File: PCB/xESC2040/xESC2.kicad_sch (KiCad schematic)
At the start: 31 parts, among them J1 Conn_01x06_Male, J2 U254-051T-4BH83-F1S, J3 Conn_01x05_Male, J4 Conn_01x05_Male

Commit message: Change part for J5 to be a 9 pin header so can be soldered along with J1 to ease assembly - J1 marked as DNP
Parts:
- J1: Config (none) -> do not place
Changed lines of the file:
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@@
+      (effects (font (size 1.27 1.27)) hide)
+    )
+    (property "Config" "do not place" (id 7) (at 21.59 115.57 0)
       (effects (font (size 1.27 1.27)) hide)
     )

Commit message: Fixed #5
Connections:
- net +3V3: now also R12.1, R8.1, R9.1
- net +5V: no longer R12.1, R8.1, R9.1
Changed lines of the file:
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@@
   (junction (at 48.26 53.34) (diameter 0) (color 0 0 0 0)
   )
+  (junction (at 36.83 95.25) (diameter 0) (color 0 0 0 0)
+  )
   (junction (at 129.54 168.91) (diameter 0) (color 0 0 0 0)
   )
@@
   )
   (junction (at 52.07 120.65) (diameter 0) (color 0 0 0 0)
-  )
-  (junction (at 31.75 95.25) (diameter 0) (color 0 0 0 0)
   )
   (junction (at 46.99 95.25) (diameter 0) (color 0 0 0 0)
@@
     (stroke (width 0) (type default) (color 0 0 0 0))
   )
-  (wire (pts (xy 31.75 95.25) (xy 31.75 90.17))
-    (stroke (width 0) (type default) (color 0 0 0 0))
-  )
   (wire (pts (xy 90.805 93.345) (xy 115.57 93.345))
     (stroke (width 0) (type default) (color 0 0 0 0))
@@
     (stroke (width 0) (type default) (color 0 0 0 0))
   )
-  (wire (pts (xy 31.75 95.25) (xy 41.91 95.25))
-    (stroke (width 0) (type default) (color 0 0 0 0))
-  )
   (wire (pts (xy 217.17 39.37) (xy 223.52 39.37))
     (stroke (width 0) (type default) (color 0 0 0 0))
@@
     (stroke (width 0) (type default) (color 0 0 0 0))
   )
+  (wire (pts (xy 36.83 95.25) (xy 41.91 95.25))
+    (stroke (width 0) (type default) (color 0 0 0 0))
+  )
   (wire (pts (xy 129.54 158.75) (xy 129.54 154.94))
     (stroke (width 0) (type default) (color 0 0 0 0))
@@
     (stroke (width 0) (type default) (color 0 0 0 0))
   )
+  (wire (pts (xy 36.83 95.25) (xy 36.83 90.17))
+    (stroke (width 0) (type default) (color 0 0 0 0))
+  )
   (wire (pts (xy 48.26 53.34) (xy 48.26 59.69))
     (stroke (width 0) (type default) (color 0 0 0 0))
@@
     (stroke (width 0) (type default) (color 0 0 0 0))
   )
-  (wire (pts (xy 36.83 104.14) (xy 36.83 90.17))
+  (wire (pts (xy 36.83 104.14) (xy 36.83 95.25))
     (stroke (width 0) (type default) (color 0 0 0 0))
   )
@@
     (stroke (width 0) (type default) (color 0 0 0 0))
   )
-  (wire (pts (xy 31.75 110.49) (xy 31.75 95.25))
-    (stroke (width 0) (type default) (color 0 0 0 0))
-  )
+  (wire (pts (xy 31.75 90.17) (xy 31.75 110.49))
+    (stroke (width 0) (type default) (color 0 0 0 0))
+  )

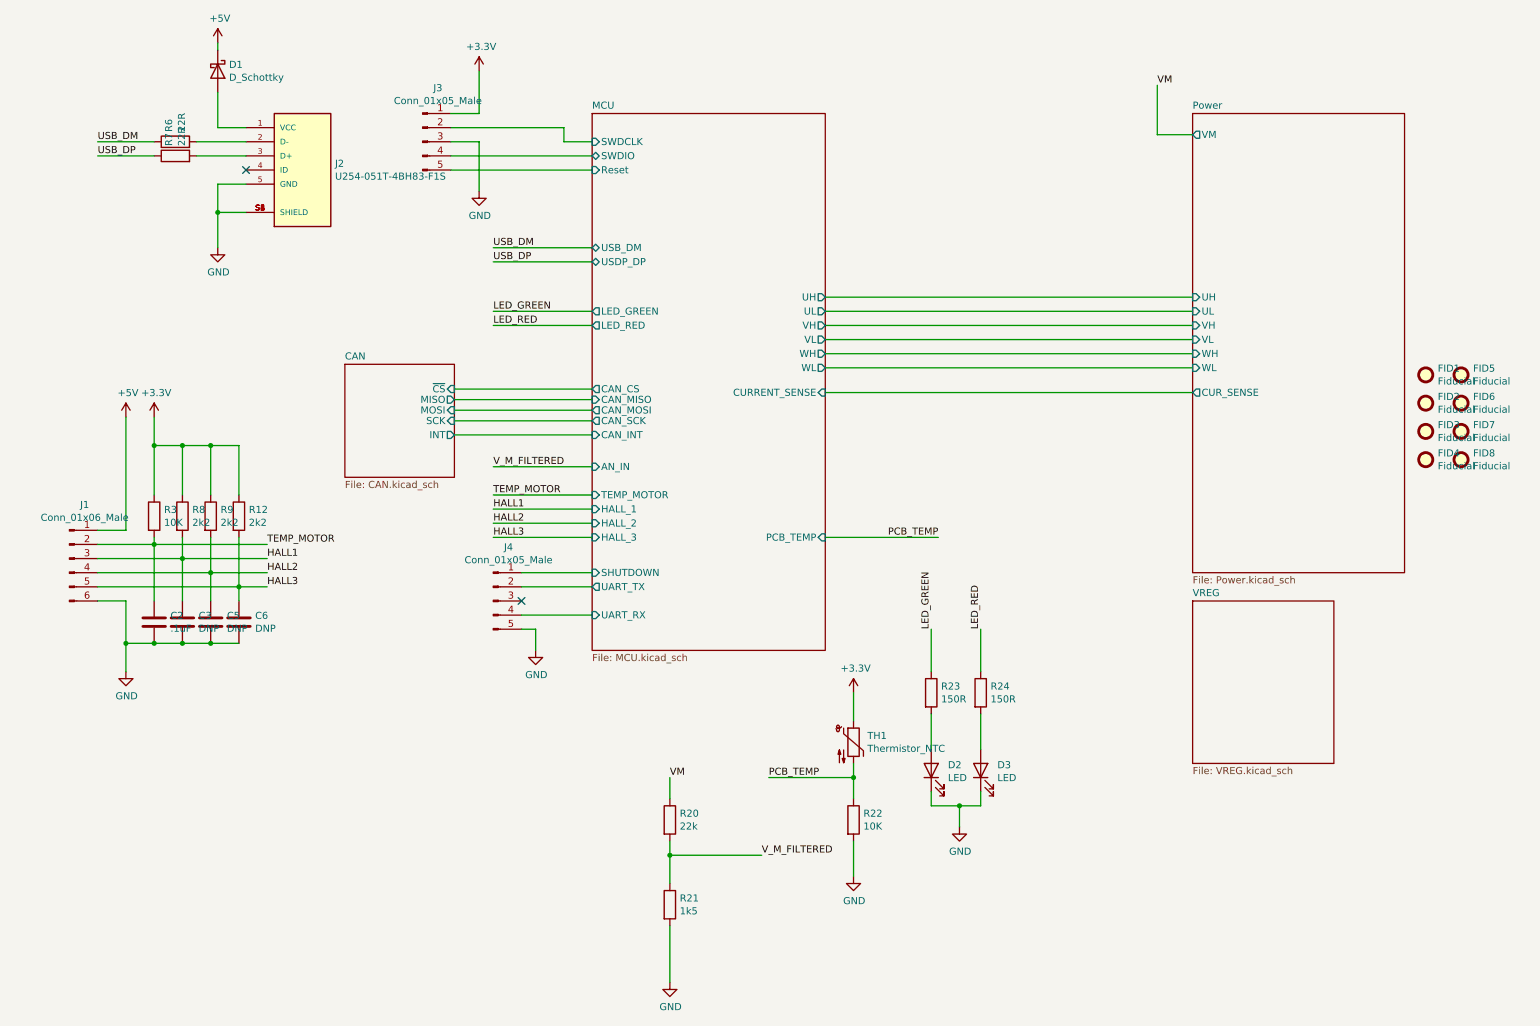
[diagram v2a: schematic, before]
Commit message: Merge J5 and J1 into one connector - no pinout changes or connector move
With J5 gone had kicad redo  reference designators - hope that's ok
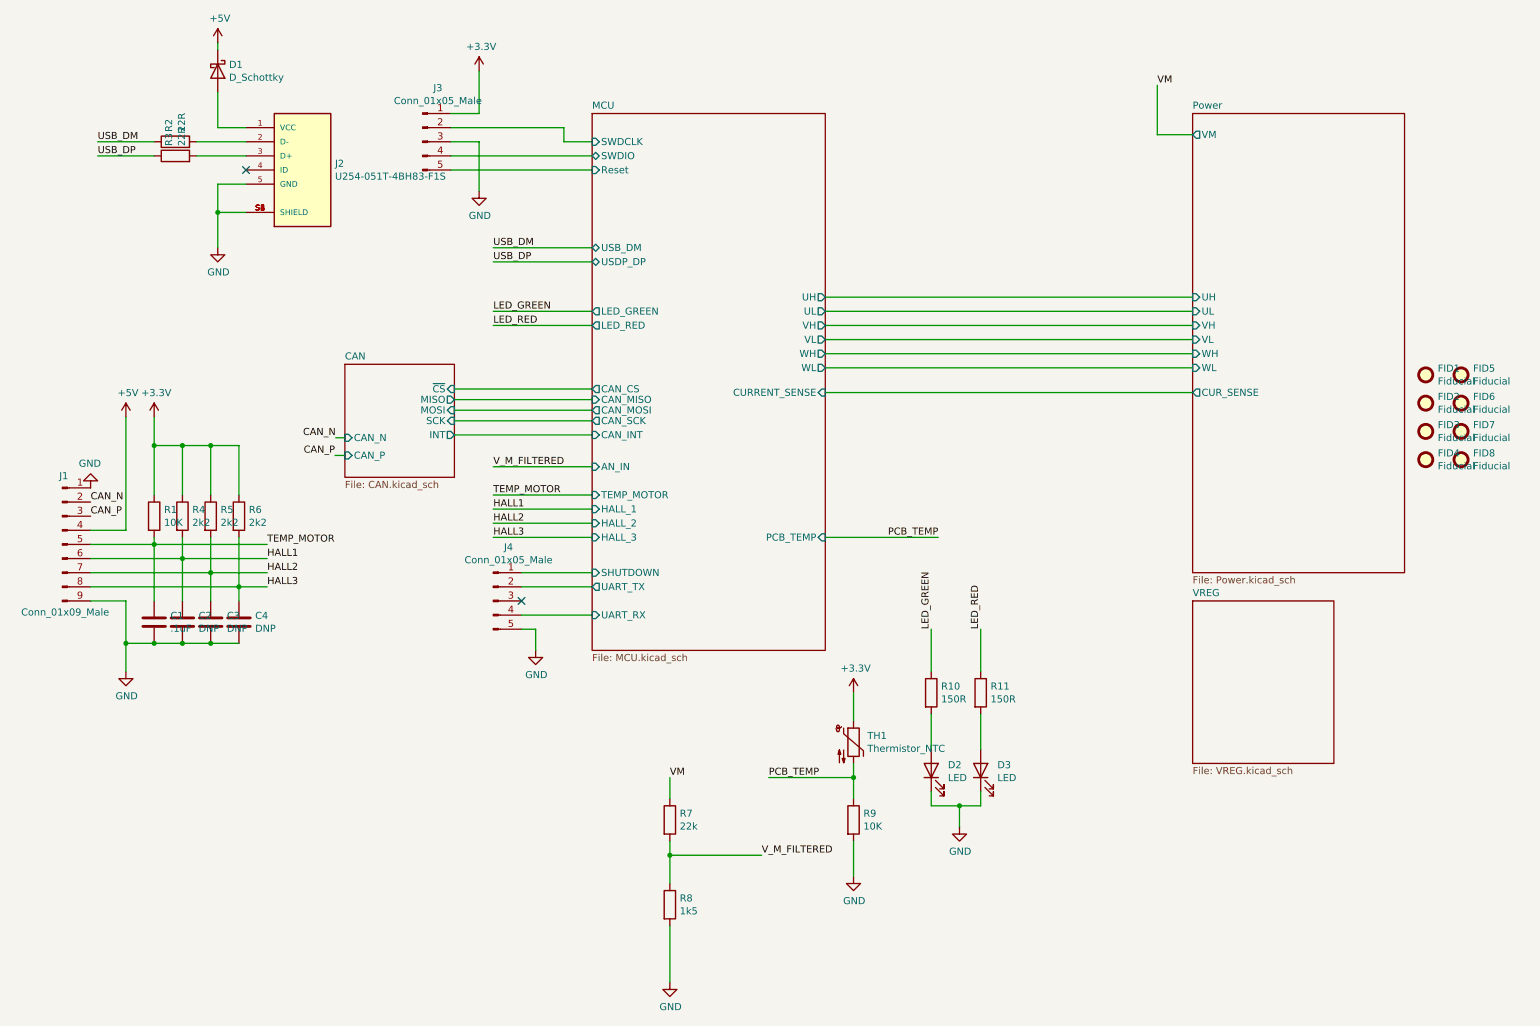
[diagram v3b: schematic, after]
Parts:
- removed J1: Conn_01x06_Male, Connector_PinHeader_2.54mm:PinHeader_1x06_P2.54mm_Vertical, symbol Connector:Conn_01x06_Male
- added J1: Conn_01x09_Male, Connector_PinHeader_2.54mm:PinHeader_1x09_P2.54mm_Vertical, symbol Connector:Conn_01x09_Male
- renumbered C2 to C1, C3 to C2, C5 to C3, C6 to C4, R3 to R1, R23 to R10, R24 to R11, R6 to R2, R7 to R3, R8 to R4, R9 to R5, R12 to R6, R20 to R7, R21 to R8, R22 to R9
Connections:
- net +5V: now also J1.4 (Pin_4)
- net GND: now also J1.1 (Pin_1), J1.9 (Pin_9)
- net HALL1: now also J1.6 (Pin_6)
- net HALL2: now also J1.7 (Pin_7)
- net HALL3: now also J1.8 (Pin_8)
- net TEMP_MOTOR: now also J1.5 (Pin_5)
- new net CAN_N: J1.2 (Pin_2)
- new net CAN_P: J1.3 (Pin_3)
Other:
- sheet CAN ports: added CAN_N, CAN_P; removed none

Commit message: BoM data updates
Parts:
- R1, R9: Digikey RC0603FR-0710KL -> 311-10.0KHRCT-ND; Part Number 311-10.0KHRCT-ND -> RC0603FR-0710KL
- R10, R11: Digikey RC0603FR-07150RL -> 311-150HRCT-ND; Part Number 311-150HRCT-ND -> RC0603FR-07150RL
- R2, R3: Digikey RMCF0603FT22R0 -> RMCF0603FT22R0CT-ND; Part Number RMCF0603FT22R0CT-ND -> RMCF0603FT22R0
- R4, R5, R6: Digikey RC0603FR-072K2L -> 311-2.20KHRCT-ND; Part Number 311-2.20KHRCT-ND -> RC0603FR-072K2L
- R7: Digikey RMCF0603FT22K0 -> RMCF0603FT22K0CT-ND; Part Number RMCF0603FT22K0CT-ND -> RMCF0603FT22K0
- R8: Digikey RC0603FR-071K5L -> 311-1.50KHRCT-ND; Part Number 311-1.50KHRCT-ND -> RC0603FR-071K5L
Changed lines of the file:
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@@
       (effects (font (size 1.27 1.27)) hide)
     )
-    (property "Digikey" "RC0603FR-0710KL" (id 4) (at 36.83 107.95 0)
-      (effects (font (size 1.27 1.27)) hide)
-    )
-    (property "Part Number" "311-10.0KHRCT-ND" (id 5) (at 36.83 107.95 0)
+    (property "Digikey" "311-10.0KHRCT-ND" (id 4) (at 36.83 107.95 0)
+      (effects (font (size 1.27 1.27)) hide)
+    )
+    (property "Part Number" "RC0603FR-0710KL" (id 5) (at 36.83 107.95 0)
       (effects (font (size 1.27 1.27)) hide)
     )
@@
       (effects (font (size 1.27 1.27)) hide)
     )
-    (property "Digikey" "RC0603FR-072K2L" (id 4) (at 41.91 107.95 0)
-      (effects (font (size 1.27 1.27)) hide)
-    )
-    (property "Part Number" "311-2.20KHRCT-ND" (id 5) (at 41.91 107.95 0)
+    (property "Digikey" "311-2.20KHRCT-ND" (id 4) (at 41.91 107.95 0)
+      (effects (font (size 1.27 1.27)) hide)
+    )
+    (property "Part Number" "RC0603FR-072K2L" (id 5) (at 41.91 107.95 0)
       (effects (font (size 1.27 1.27)) hide)
     )
@@
       (effects (font (size 1.27 1.27)) hide)
     )
-    (property "Digikey" "RC0603FR-072K2L" (id 4) (at 46.99 107.95 0)
-      (effects (font (size 1.27 1.27)) hide)
-    )
-    (property "Part Number" "311-2.20KHRCT-ND" (id 5) (at 46.99 107.95 0)
+    (property "Digikey" "311-2.20KHRCT-ND" (id 4) (at 46.99 107.95 0)
+      (effects (font (size 1.27 1.27)) hide)
+    )
+    (property "Part Number" "RC0603FR-072K2L" (id 5) (at 46.99 107.95 0)
       (effects (font (size 1.27 1.27)) hide)
     )
@@
       (effects (font (size 1.27 1.27)) hide)
     )
-    (property "Digikey" "RC0603FR-072K2L" (id 4) (at 52.07 107.95 0)
-      (effects (font (size 1.27 1.27)) hide)
-    )
-    (property "Part Number" "311-2.20KHRCT-ND" (id 5) (at 52.07 107.95 0)
+    (property "Digikey" "311-2.20KHRCT-ND" (id 4) (at 52.07 107.95 0)
+      (effects (font (size 1.27 1.27)) hide)
+    )
+    (property "Part Number" "RC0603FR-072K2L" (id 5) (at 52.07 107.95 0)
       (effects (font (size 1.27 1.27)) hide)
     )
@@
       (effects (font (size 1.27 1.27)) hide)
     )
-    (property "Digikey" "RMCF0603FT22K0" (id 4) (at 129.54 162.56 0)
-      (effects (font (size 1.27 1.27)) hide)
-    )
-    (property "Part Number" "RMCF0603FT22K0CT-ND" (id 5) (at 129.54 162.56 0)
+    (property "Digikey" "RMCF0603FT22K0CT-ND" (id 4) (at 129.54 162.56 0)
+      (effects (font (size 1.27 1.27)) hide)
+    )
+    (property "Part Number" "RMCF0603FT22K0" (id 5) (at 129.54 162.56 0)
       (effects (font (size 1.27 1.27)) hide)
     )
@@
       (effects (font (size 1.27 1.27)) hide)
     )
-    (property "Digikey" "RC0603FR-071K5L" (id 4) (at 129.54 177.8 0)
-      (effects (font (size 1.27 1.27)) hide)
-    )
-    (property "Part Number" "311-1.50KHRCT-ND" (id 5) (at 129.54 177.8 0)
+    (property "Digikey" "311-1.50KHRCT-ND" (id 4) (at 129.54 177.8 0)
+      (effects (font (size 1.27 1.27)) hide)
+    )
+    (property "Part Number" "RC0603FR-071K5L" (id 5) (at 129.54 177.8 0)
       (effects (font (size 1.27 1.27)) hide)
     )
@@
       (effects (font (size 1.27 1.27)) hide)
     )
-    (property "Digikey" "RMCF0603FT22R0" (id 4) (at 40.64 43.18 0)
-      (effects (font (size 1.27 1.27)) hide)
-    )
-    (property "Part Number" "RMCF0603FT22R0CT-ND" (id 5) (at 40.64 43.18 0)
+    (property "Digikey" "RMCF0603FT22R0CT-ND" (id 4) (at 40.64 43.18 0)
+      (effects (font (size 1.27 1.27)) hide)
+    )
+    (property "Part Number" "RMCF0603FT22R0" (id 5) (at 40.64 43.18 0)
       (effects (font (size 1.27 1.27)) hide)
     )
@@
       (effects (font (size 1.27 1.27)) hide)
     )
-    (property "Digikey" "RMCF0603FT22R0" (id 4) (at 40.64 40.64 0)
-      (effects (font (size 1.27 1.27)) hide)
-    )
-    (property "Part Number" "RMCF0603FT22R0CT-ND" (id 5) (at 40.64 40.64 0)
+    (property "Digikey" "RMCF0603FT22R0CT-ND" (id 4) (at 40.64 40.64 0)
+      (effects (font (size 1.27 1.27)) hide)
+    )
+    (property "Part Number" "RMCF0603FT22R0" (id 5) (at 40.64 40.64 0)
       (effects (font (size 1.27 1.27)) hide)
     )
@@
       (effects (font (size 1.27 1.27)) hide)
     )
-    (property "Digikey" "RC0603FR-07150RL" (id 4) (at 176.53 139.7 0)
-      (effects (font (size 1.27 1.27)) hide)
-    )
-    (property "Part Number" "311-150HRCT-ND" (id 5) (at 176.53 139.7 0)
+    (property "Digikey" "311-150HRCT-ND" (id 4) (at 176.53 139.7 0)
+      (effects (font (size 1.27 1.27)) hide)
+    )
+    (property "Part Number" "RC0603FR-07150RL" (id 5) (at 176.53 139.7 0)
       (effects (font (size 1.27 1.27)) hide)
     )
@@
       (effects (font (size 1.27 1.27)) hide)
     )
-    (property "Digikey" "RC0603FR-0710KL" (id 4) (at 162.56 162.56 0)
-      (effects (font (size 1.27 1.27)) hide)
-    )
-    (property "Part Number" "311-10.0KHRCT-ND" (id 5) (at 162.56 162.56 0)
+    (property "Digikey" "311-10.0KHRCT-ND" (id 4) (at 162.56 162.56 0)
+      (effects (font (size 1.27 1.27)) hide)
+    )
+    (property "Part Number" "RC0603FR-0710KL" (id 5) (at 162.56 162.56 0)
       (effects (font (size 1.27 1.27)) hide)
     )
@@
       (effects (font (size 1.27 1.27)) hide)
     )
-    (property "Digikey" "RC0603FR-07150RL" (id 4) (at 185.42 139.7 0)
-      (effects (font (size 1.27 1.27)) hide)
-    )
-    (property "Part Number" "311-150HRCT-ND" (id 5) (at 185.42 139.7 0)
-      (effects (font (size 1.27 1.27)) hide)
-    )
+    (property "Digikey" "311-150HRCT-ND" (id 4) (at 185.42 139.7 0)
+      (effects (font (size 1.27 1.27)) hide)
+    )
+    (property "Part Number" "RC0603FR-07150RL" (id 5) (at 185.42 139.7 0)
+      (effects (font (size 1.27 1.27)) hide)
+    )

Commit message: wip
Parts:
- C1: Digikey 490-1331-1-ND -> 1276-1935-1-ND
- D2: value LED -> LED GREEN
- D3: value LED -> LED RED
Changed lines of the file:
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@@
       (effects (font (size 1.27 1.27)) hide)
     )
-    (property "Digikey" "490-1331-1-ND" (id 4) (at 36.83 127 0)
+    (property "Digikey" "1276-1935-1-ND" (id 4) (at 36.83 127 0)
       (effects (font (size 1.27 1.27)) hide)
     )
@@
       (effects (font (size 1.27 1.27)) (justify right))
     )
-    (property "Value" "LED" (id 1) (at 179.5272 154.9908 90)
+    (property "Value" "LED GREEN" (id 1) (at 179.5272 154.9908 90)
       (effects (font (size 1.27 1.27)) (justify right))
     )
@@
       (effects (font (size 1.27 1.27)) (justify right))
     )
-    (property "Value" "LED" (id 1) (at 188.4172 154.9908 90)
+    (property "Value" "LED RED" (id 1) (at 188.4172 154.9908 90)
       (effects (font (size 1.27 1.27)) (justify right))
     )
@@
     )
     (path "/00000000-0000-0000-0000-000061a3f4e8/b5bb664c-0ca2-4020-8c91-65a02cddeb94"
-      (reference "C20") (unit 1) (value "TODO") (footprint "Capacitor_SMD:C_0603_1608Metric")
+      (reference "C20") (unit 1) (value ".1uF") (footprint "Capacitor_SMD:C_0603_1608Metric")
     )
     (path "/00000000-0000-0000-0000-000061a3f4e8/00000000-0000-0000-0000-000061a4478e"
-      (reference "C21") (unit 1) (value "TODO") (footprint "Capacitor_SMD:C_0603_1608Metric")
+      (reference "C21") (unit 1) (value "470nF{slash}16V") (footprint "Capacitor_SMD:C_0603_1608Metric")
     )
     (path "/00000000-0000-0000-0000-000061a3f4e8/00000000-0000-0000-0000-000061a4b0d8"
-      (reference "C22") (unit 1) (value "TODO") (footprint "Capacitor_SMD:C_0603_1608Metric")
+      (reference "C22") (unit 1) (value "470nF{slash}16V") (footprint "Capacitor_SMD:C_0603_1608Metric")
     )
     (path "/00000000-0000-0000-0000-000061a3f4e8/00000000-0000-0000-0000-000061a4bb26"
-      (reference "C23") (unit 1) (value "TODO") (footprint "Capacitor_SMD:C_0603_1608Metric")
+      (reference "C23") (unit 1) (value "470nF{slash}16V") (footprint "Capacitor_SMD:C_0603_1608Metric")
     )
     (path "/00000000-0000-0000-0000-000061e7227a/00000000-0000-0000-0000-000061e808d2"
-      (reference "C24") (unit 1) (value "10uF/16V") (footprint "Capacitor_SMD:C_0603_1608Metric")
+      (reference "C24") (unit 1) (value "4.7uF{slash}16V") (footprint "Capacitor_SMD:C_0603_1608Metric")
     )
     (path "/00000000-0000-0000-0000-000061e7227a/6c7a9801-3387-4fa6-ac74-fb6a0114bfa0"
-      (reference "C25") (unit 1) (value "10uF/16V") (footprint "Capacitor_SMD:C_0603_1608Metric")
+      (reference "C25") (unit 1) (value "4.7uF{slash}16V") (footprint "Capacitor_SMD:C_0603_1608Metric")
     )
     (path "/00000000-0000-0000-0000-000061a3f4e8/00000000-0000-0000-0000-000061a57dd0/00000000-0000-0000-0000-000061a5475a"
@@
     )
     (path "/00000000-0000-0000-0000-000061e2e723"
-      (reference "D2") (unit 1) (value "LED") (footprint "LED_SMD:LED_0603_1608Metric")
+      (reference "D2") (unit 1) (value "LED GREEN") (footprint "LED_SMD:LED_0603_1608Metric")
     )
     (path "/00000000-0000-0000-0000-000061e3947a"
-      (reference "D3") (unit 1) (value "LED") (footprint "LED_SMD:LED_0603_1608Metric")
+      (reference "D3") (unit 1) (value "LED RED") (footprint "LED_SMD:LED_0603_1608Metric")
     )
     (path "/00000000-0000-0000-0000-00006251351c"
@@
     )
     (path "/00000000-0000-0000-0000-000061a3f4e8/363f2f39-147c-4fe7-ae7c-93ceb80426de"
-      (reference "R17") (unit 1) (value "TODO") (footprint "Resistor_SMD:R_0603_1608Metric")
+      (reference "R17") (unit 1) (value "DNP") (footprint "Resistor_SMD:R_0603_1608Metric")
     )
     (path "/00000000-0000-0000-0000-000061a3f4e8/c6c90108-6f77-4a49-81b5-720115855806"
-      (reference "R18") (unit 1) (value "33mR") (footprint "Resistor_SMD:R_2512_6332Metric")
+      (reference "R18") (unit 1) (value "3mR") (footprint "Resistor_SMD:R_2512_6332Metric")
     )
     (path "/00000000-0000-0000-0000-000061a3f4e8/00000000-0000-0000-0000-000061a57dd0/00000000-0000-0000-0000-000061a4c174"
@@
     )
     (path "/00000000-0000-0000-0000-000061a3f4e8/6e53077b-00a7-42fa-bde8-29bc57990250"
-      (reference "U4") (unit 1) (value "INA180A3IDBVR") (footprint "INA180:SOT95P280X145-5N")
+      (reference "U4") (unit 1) (value "INA180A4") (footprint "INA180:SOT95P280X145-5N")
     )
     (path "/00000000-0000-0000-0000-000061e7227a/00000000-0000-0000-0000-000062018de5"
@@
     )
     (path "/00000000-0000-0000-0000-000061ac26fb/cad27c59-62e5-414e-946c-08aafd176309"
-      (reference "Y1") (unit 1) (value "Crystal_GND24") (footprint "Crystal:Crystal_SMD_3225-4Pin_3.2x2.5mm")
+      (reference "Y1") (unit 1) (value "12MHz") (footprint "Crystal:Crystal_SMD_3225-4Pin_3.2x2.5mm")
     )
     (path "/d5d37f5b-4bf9-4532-a06e-fdd7971cf83d/2d8aed8e-5480-4471-bae1-c9c35cebe5ca"
